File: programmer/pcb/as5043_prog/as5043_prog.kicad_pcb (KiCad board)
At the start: 2 copper layers, 11 parts, among them J1 Conn_01x03_Male, J2 Conn_01x03_Male, Q1 8550SS, Q2 8550SS, U1 ATtiny13A-PU

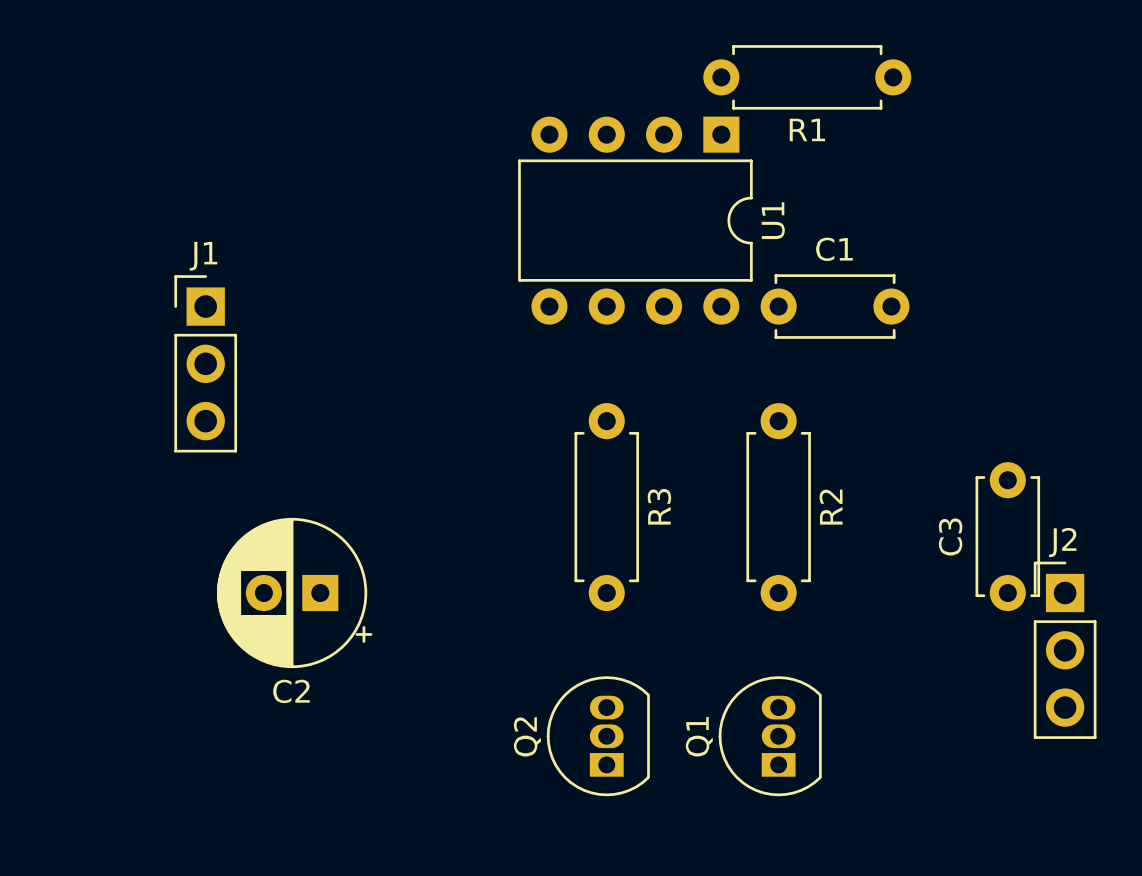
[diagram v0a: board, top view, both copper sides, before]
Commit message: Added some small changes to the programmer electronics
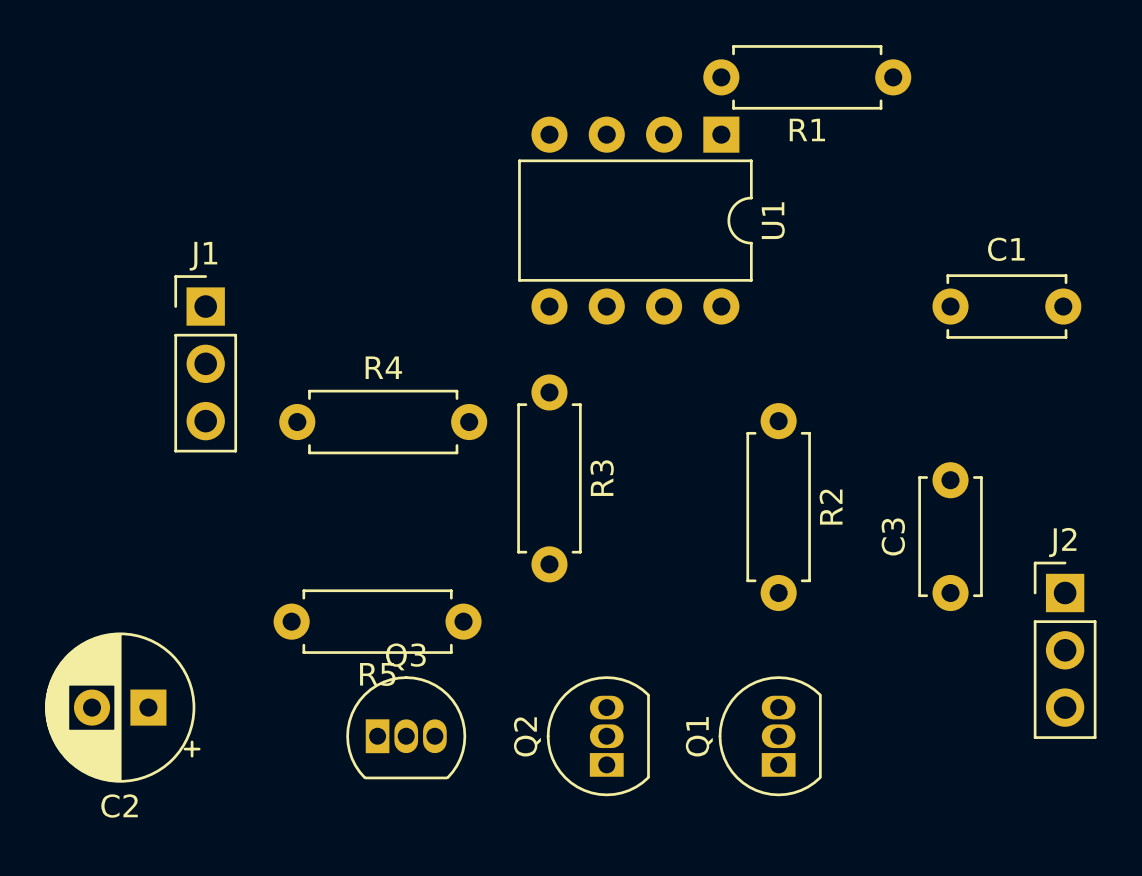
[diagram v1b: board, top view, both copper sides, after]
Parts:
- added Q3: BC547, Package_TO_SOT_THT:TO-92_Inline, F.Cu at (119.4, 82.5)
- added R4: 10K, Resistor_THT:R_Axial_DIN0207_L6.3mm_D2.5mm_P7.62mm_Horizontal, F.Cu at (115.8, 68.6)
- added R5: 1K, Resistor_THT:R_Axial_DIN0207_L6.3mm_D2.5mm_P7.62mm_Horizontal, F.Cu at (123.2, 77.5)
- moved C2 9.16 mm to (109.2, 81.3)
- moved C1 7.62 mm to (144.8, 63.5)
- moved R3 2.84 mm to (127.0, 67.3)
- moved C3 2.54 mm to (144.8, 76.2)
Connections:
- R3 pad 2: Net-(Q2-Pad3) -> Net-(Q3-Pad2)
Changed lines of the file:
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@@
     (tracks 0)
     (zones 0)
-    (modules 11)
-    (nets 13)
+    (modules 14)
+    (nets 15)
   )
   (page A4)
@@
   (net 11 /PROG_HV)
   (net 12 "Net-(U1-Pad3)")
+  (net 13 "Net-(Q3-Pad1)")
+  (net 14 "Net-(Q3-Pad2)")
   (net_class Default "This is the default net class."
     (clearance 0.2)
@@
     (add_net "Net-(Q1-Pad3)")
     (add_net "Net-(Q2-Pad3)")
+    (add_net "Net-(Q3-Pad1)")
+    (add_net "Net-(Q3-Pad2)")
     (add_net "Net-(R1-Pad2)")
     (add_net "Net-(U1-Pad3)")
+  )
+  (module Resistor_THT:R_Axial_DIN0207_L6.3mm_D2.5mm_P7.62mm_Horizontal (layer F.Cu)
+    (at 123.19 77.47 180)
+    (descr "Resistor, Axial_DIN0207 series, Axial, Horizontal, pin pitch=7.62mm, 0.25W = 1/4W, length*diameter=6.3*2.5mm^2, http://cdn-reichelt.de/documents/datenblatt/B400/1_4W%23YAG.pdf")
+    (tags "Resistor Axial_DIN0207 series Axial Horizontal pin pitch 7.62mm 0.25W = 1/4W length 6.3mm diameter 2.5mm")
+    (fp_text reference R5 (at 3.81 -2.37) (layer F.SilkS)
+      (effects (font (size 1 1) (thickness 0.15)))
+    )
+    (fp_text value 1K (at 3.81 2.37) (layer F.Fab)
+      (effects (font (size 1 1) (thickness 0.15)))
+    )
+    (fp_text user %R (at 3.81 0) (layer F.Fab)
+      (effects (font (size 1 1) (thickness 0.15)))
+    )
+    (fp_line (start 0.66 -1.25) (end 0.66 1.25) (layer F.Fab) (width 0.1))
+    (fp_line (start 0.66 1.25) (end 6.96 1.25) (layer F.Fab) (width 0.1))
+    (fp_line (start 6.96 1.25) (end 6.96 -1.25) (layer F.Fab) (width 0.1))
+    (fp_line (start 6.96 -1.25) (end 0.66 -1.25) (layer F.Fab) (width 0.1))
+    (fp_line (start 0 0) (end 0.66 0) (layer F.Fab) (width 0.1))
+    (fp_line (start 7.62 0) (end 6.96 0) (layer F.Fab) (width 0.1))
+    (fp_line (start 0.54 -1.04) (end 0.54 -1.37) (layer F.SilkS) (width 0.12))
+    (fp_line (start 0.54 -1.37) (end 7.08 -1.37) (layer F.SilkS) (width 0.12))
+    (fp_line (start 7.08 -1.37) (end 7.08 -1.04) (layer F.SilkS) (width 0.12))
+    (fp_line (start 0.54 1.04) (end 0.54 1.37) (layer F.SilkS) (width 0.12))
+    (fp_line (start 0.54 1.37) (end 7.08 1.37) (layer F.SilkS) (width 0.12))
+    (fp_line (start 7.08 1.37) (end 7.08 1.04) (layer F.SilkS) (width 0.12))
+    (fp_line (start -1.05 -1.5) (end -1.05 1.5) (layer F.CrtYd) (width 0.05))
+    (fp_line (start -1.05 1.5) (end 8.67 1.5) (layer F.CrtYd) (width 0.05))
+    (fp_line (start 8.67 1.5) (end 8.67 -1.5) (layer F.CrtYd) (width 0.05))
+    (fp_line (start 8.67 -1.5) (end -1.05 -1.5) (layer F.CrtYd) (width 0.05))
+    (pad 2 thru_hole oval (at 7.62 0 180) (size 1.6 1.6) (drill 0.8) (layers *.Cu *.Mask)
+      (net 8 "Net-(Q2-Pad3)"))
+    (pad 1 thru_hole circle (at 0 0 180) (size 1.6 1.6) (drill 0.8) (layers *.Cu *.Mask)
+      (net 13 "Net-(Q3-Pad1)"))
+    (model ${KISYS3DMOD}/Resistor_THT.3dshapes/R_Axial_DIN0207_L6.3mm_D2.5mm_P7.62mm_Horizontal.wrl
+      (at (xyz 0 0 0))
+      (scale (xyz 1 1 1))
+      (rotate (xyz 0 0 0))
+    )
+  )
+  (module Resistor_THT:R_Axial_DIN0207_L6.3mm_D2.5mm_P7.62mm_Horizontal (layer F.Cu)
+    (at 115.82 68.62)
+    (descr "Resistor, Axial_DIN0207 series, Axial, Horizontal, pin pitch=7.62mm, 0.25W = 1/4W, length*diameter=6.3*2.5mm^2, http://cdn-reichelt.de/documents/datenblatt/B400/1_4W%23YAG.pdf")
+    (tags "Resistor Axial_DIN0207 series Axial Horizontal pin pitch 7.62mm 0.25W = 1/4W length 6.3mm diameter 2.5mm")
+    (fp_text reference R4 (at 3.81 -2.37) (layer F.SilkS)
+      (effects (font (size 1 1) (thickness 0.15)))
+    )
+    (fp_text value 10K (at 3.81 2.37) (layer F.Fab)
+      (effects (font (size 1 1) (thickness 0.15)))
+    )
+    (fp_text user %R (at 3.81 0) (layer F.Fab)
+      (effects (font (size 1 1) (thickness 0.15)))
+    )
+    (fp_line (start 0.66 -1.25) (end 0.66 1.25) (layer F.Fab) (width 0.1))
+    (fp_line (start 0.66 1.25) (end 6.96 1.25) (layer F.Fab) (width 0.1))
+    (fp_line (start 6.96 1.25) (end 6.96 -1.25) (layer F.Fab) (width 0.1))
+    (fp_line (start 6.96 -1.25) (end 0.66 -1.25) (layer F.Fab) (width 0.1))
+    (fp_line (start 0 0) (end 0.66 0) (layer F.Fab) (width 0.1))
+    (fp_line (start 7.62 0) (end 6.96 0) (layer F.Fab) (width 0.1))
+    (fp_line (start 0.54 -1.04) (end 0.54 -1.37) (layer F.SilkS) (width 0.12))
+    (fp_line (start 0.54 -1.37) (end 7.08 -1.37) (layer F.SilkS) (width 0.12))
+    (fp_line (start 7.08 -1.37) (end 7.08 -1.04) (layer F.SilkS) (width 0.12))
+    (fp_line (start 0.54 1.04) (end 0.54 1.37) (layer F.SilkS) (width 0.12))
+    (fp_line (start 0.54 1.37) (end 7.08 1.37) (layer F.SilkS) (width 0.12))
+    (fp_line (start 7.08 1.37) (end 7.08 1.04) (layer F.SilkS) (width 0.12))
+    (fp_line (start -1.05 -1.5) (end -1.05 1.5) (layer F.CrtYd) (width 0.05))
+    (fp_line (start -1.05 1.5) (end 8.67 1.5) (layer F.CrtYd) (width 0.05))
+    (fp_line (start 8.67 1.5) (end 8.67 -1.5) (layer F.CrtYd) (width 0.05))
+    (fp_line (start 8.67 -1.5) (end -1.05 -1.5) (layer F.CrtYd) (width 0.05))
+    (pad 2 thru_hole oval (at 7.62 0) (size 1.6 1.6) (drill 0.8) (layers *.Cu *.Mask)
+      (net 13 "Net-(Q3-Pad1)"))
+    (pad 1 thru_hole circle (at 0 0) (size 1.6 1.6) (drill 0.8) (layers *.Cu *.Mask)
+      (net 3 +7.5V))
+    (model ${KISYS3DMOD}/Resistor_THT.3dshapes/R_Axial_DIN0207_L6.3mm_D2.5mm_P7.62mm_Horizontal.wrl
+      (at (xyz 0 0 0))
+      (scale (xyz 1 1 1))
+      (rotate (xyz 0 0 0))
+    )
+  )
+  (module Package_TO_SOT_THT:TO-92_Inline (layer F.Cu)
+    (at 119.38 82.55)
+    (descr "TO-92 leads in-line, narrow, oval pads, drill 0.75mm (see NXP sot054_po.pdf)")
+    (tags "to-92 sc-43 sc-43a sot54 PA33 transistor")
+    (fp_text reference Q3 (at 1.27 -3.56) (layer F.SilkS)
+      (effects (font (size 1 1) (thickness 0.15)))
+    )
+    (fp_text value BC547 (at 1.27 2.79) (layer F.Fab)
+      (effects (font (size 1 1) (thickness 0.15)))
+    )
+    (fp_arc (start 1.27 0) (end 1.27 -2.6) (angle 135) (layer F.SilkS) (width 0.12))
+    (fp_arc (start 1.27 0) (end 1.27 -2.48) (angle -135) (layer F.Fab) (width 0.1))
+    (fp_arc (start 1.27 0) (end 1.27 -2.6) (angle -135) (layer F.SilkS) (width 0.12))
+    (fp_arc (start 1.27 0) (end 1.27 -2.48) (angle 135) (layer F.Fab) (width 0.1))
+    (fp_text user %R (at 1.27 -3.56) (layer F.Fab)
+      (effects (font (size 1 1) (thickness 0.15)))
+    )
+    (fp_line (start -0.53 1.85) (end 3.07 1.85) (layer F.SilkS) (width 0.12))
+    (fp_line (start -0.5 1.75) (end 3 1.75) (layer F.Fab) (width 0.1))
+    (fp_line (start -1.46 -2.73) (end 4 -2.73) (layer F.CrtYd) (width 0.05))
+    (fp_line (start -1.46 -2.73) (end -1.46 2.01) (layer F.CrtYd) (width 0.05))
+    (fp_line (start 4 2.01) (end 4 -2.73) (layer F.CrtYd) (width 0.05))
+    (fp_line (start 4 2.01) (end -1.46 2.01) (layer F.CrtYd) (width 0.05))
+    (pad 1 thru_hole rect (at 0 0) (size 1.05 1.5) (drill 0.75) (layers *.Cu *.Mask)
+      (net 13 "Net-(Q3-Pad1)"))
+    (pad 3 thru_hole oval (at 2.54 0) (size 1.05 1.5) (drill 0.75) (layers *.Cu *.Mask)
+      (net 1 GND))
+    (pad 2 thru_hole oval (at 1.27 0) (size 1.05 1.5) (drill 0.75) (layers *.Cu *.Mask)
+      (net 14 "Net-(Q3-Pad2)"))
+    (model ${KISYS3DMOD}/Package_TO_SOT_THT.3dshapes/TO-92_Inline.wrl
+      (at (xyz 0 0 0))
+      (scale (xyz 1 1 1))
+      (rotate (xyz 0 0 0))
+    )
   )
   (module Connector_PinHeader_2.54mm:PinHeader_1x03_P2.54mm_Vertical (layer F.Cu)
@@
   )
   (module Capacitor_THT:CP_Radial_D6.3mm_P2.50mm (layer F.Cu)
-    (at 116.84 76.2 180)
+    (at 109.22 81.28 180)
     (descr "CP, Radial series, Radial, pin pitch=2.50mm, , diameter=6.3mm, Electrolytic Capacitor")
     (tags "CP Radial series Radial pin pitch 2.50mm  diameter 6.3mm Electrolytic Capacitor")
@@
   )
   (module Resistor_THT:R_Axial_DIN0207_L6.3mm_D2.5mm_P7.62mm_Horizontal (layer F.Cu)
-    (at 129.54 68.58 270)
+    (at 127 67.31 270)
     (descr "Resistor, Axial_DIN0207 series, Axial, Horizontal, pin pitch=7.62mm, 0.25W = 1/4W, length*diameter=6.3*2.5mm^2, http://cdn-reichelt.de/documents/datenblatt/B400/1_4W%23YAG.pdf")
     (tags "Resistor Axial_DIN0207 series Axial Horizontal pin pitch 7.62mm 0.25W = 1/4W length 6.3mm diameter 2.5mm")
@@
     (fp_line (start 8.67 -1.5) (end -1.05 -1.5) (layer F.CrtYd) (width 0.05))
     (pad 2 thru_hole oval (at 7.62 0 270) (size 1.6 1.6) (drill 0.8) (layers *.Cu *.Mask)
-      (net 8 "Net-(Q2-Pad3)"))
+      (net 14 "Net-(Q3-Pad2)"))
     (pad 1 thru_hole circle (at 0 0 270) (size 1.6 1.6) (drill 0.8) (layers *.Cu *.Mask)
       (net 11 /PROG_HV))
@@
   )
   (module Capacitor_THT:C_Disc_D5.0mm_W2.5mm_P5.00mm (layer F.Cu)
-    (at 147.32 76.2 90)
+    (at 144.78 76.2 90)
     (descr "C, Disc series, Radial, pin pitch=5.00mm, , diameter*width=5*2.5mm^2, Capacitor, http://cdn-reichelt.de/documents/datenblatt/B300/DS_KERKO_TC.pdf")
     (tags "C Disc series Radial pin pitch 5.00mm  diameter 5mm width 2.5mm Capacitor")
@@
   )
   (module Capacitor_THT:C_Disc_D5.0mm_W2.5mm_P5.00mm (layer F.Cu)
-    (at 137.16 63.5)
+    (at 144.78 63.5)
     (descr "C, Disc series, Radial, pin pitch=5.00mm, , diameter*width=5*2.5mm^2, Capacitor, http://cdn-reichelt.de/documents/datenblatt/B300/DS_KERKO_TC.pdf")
     (tags "C Disc series Radial pin pitch 5.00mm  diameter 5mm width 2.5mm Capacitor")
